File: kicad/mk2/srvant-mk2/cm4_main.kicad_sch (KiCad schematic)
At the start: 71 parts, among them J10 HDMI connector, J11 USB A, J6 Conn_02x05_Odd_Even, J8 Bus_M.2_Socket_M, J9 ARJM11, U13 74AHC1G04, U14 AP22653W6, U16 FSUSB42MUX, U17 PCF85063AT/AAZ, U18 74LVC1G07SE-7, U19 TPD4EUSB30, U20 TPD4EUSB30, U21 74LVC1G07SE-7, U23 SLB9670VQ20FW785XTMA1, U24 74AHC1G08, Y3 X32K768S301

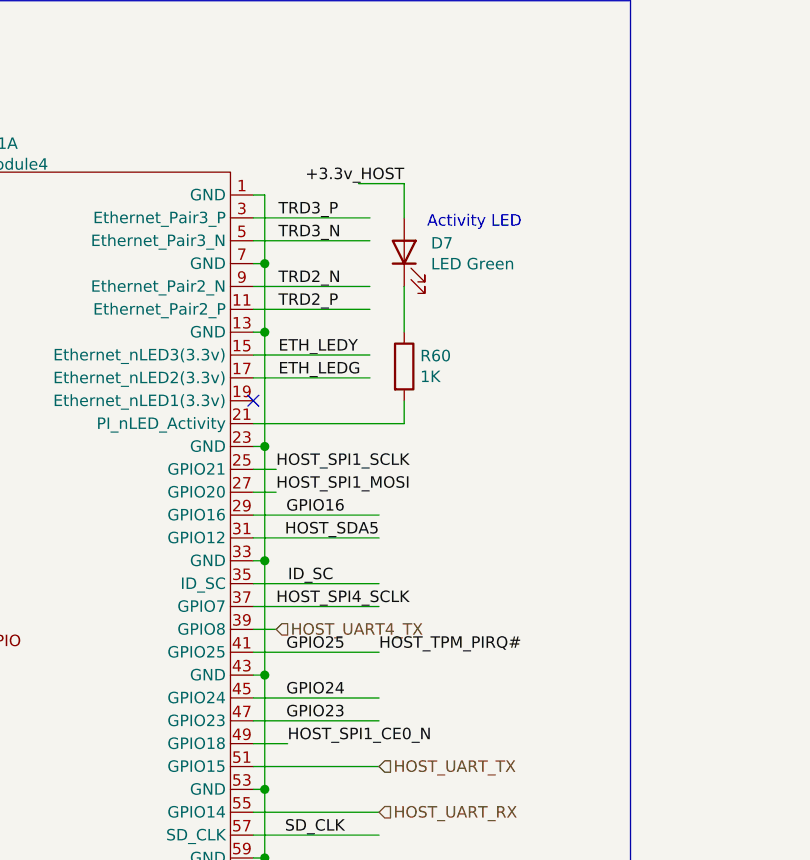
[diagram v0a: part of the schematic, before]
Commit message: reroute diff pairs
Reroute all diff pairs after another run with the jlcpcb calculator.
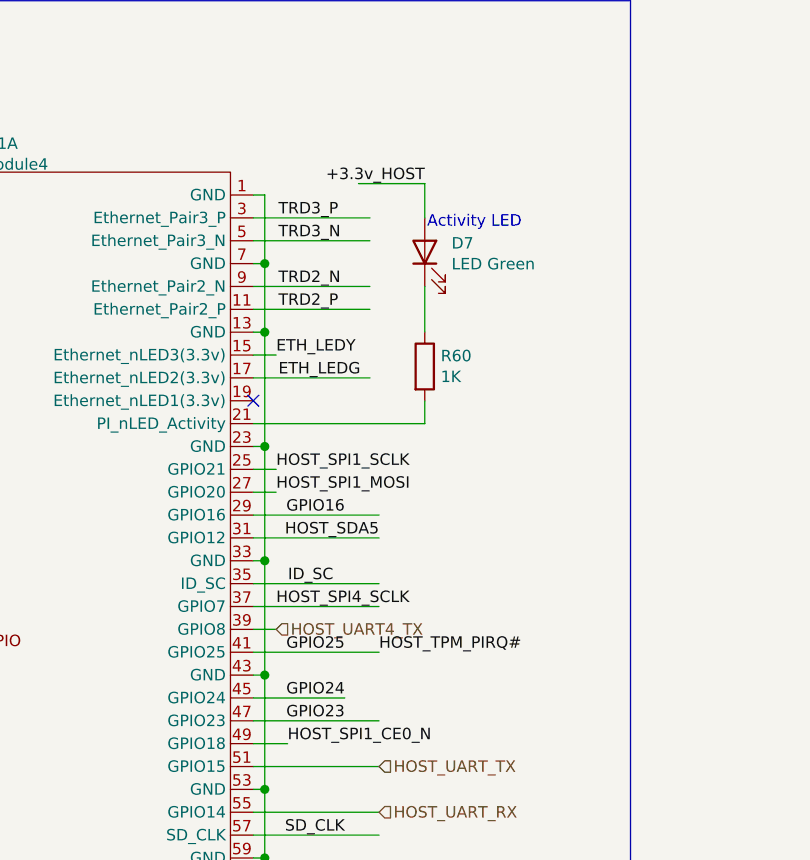
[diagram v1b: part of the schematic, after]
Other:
- moved on the sheet: D7, R60

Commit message: lot's of small updates
* fix the quartz footprint
* fix wrong inductor in pcie power unit
* fix lots of descriptions,uids
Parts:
- C102, C87, C98: Field4 Farnell -> (none); Field5 2611911 -> (none); Field6 RM EMK105 B7104KV-F -> (none); Field7 TAIYO YUDEN EUROPE GMBH -> (none); Field8 110091611 -> (none); farnell# (none) -> 3582682; manf# (none) -> GCM155R71C104KA55D; mouser# (none) -> 81-GCM155R71C104KA5D
- C42, C86, C93: farnell# (none) -> 3013481; manf# (none) -> CL21B105KAFNNNE
- C70, C75, C77, C79, C81, C83, C85, C92: Field5 490-14381-1-ND -> 490-10505-1-ND; Field6 GRM21BR71A106KA73L -> GRM21BC8YA106KE11L
- C74: Field4 Mouser -> (none); Field5 ECASD40J107M015K00 -> (none); mouser# (none) -> ECASD40J107M015K00
- C84, C91, C99: farnell# (none) -> 2812395; manf# (none) -> 885012207033
- C94: footprint Capacitor_SMD:C_0805_2012Metric -> Capacitor_SMD:C_0402_1005Metric; manf# (none) -> GRT155C81A105KE01D; mouser# (none) -> 81-GRT155C81A105KE1D
- FB8, FB9: farnell# (none) -> 4236024
- U13: farnell# (none) -> 1893806
- U14: farnell# (none) -> 3755402; manf# (none) -> AP22653W6-7
- U23: farnell# (none) -> 3404700
- U24: footprint Package_TO_SOT_SMD:SOT-23-5_HandSoldering -> Package_TO_SOT_SMD:SOT-23-5; farnell# (none) -> 3120306
- Y3: footprint Crystal:Crystal_SMD_3215-2Pin_3.2x1.5mm -> PCM_Crystal_AKL:Crystal_SMD_2012-2Pin_2.0x1.2mm; Field7 AEL -> (none); digikey# (none) -> 535-14101-2-ND; manf# (none) -> ABS06W-32.768KHZ-K-2-T

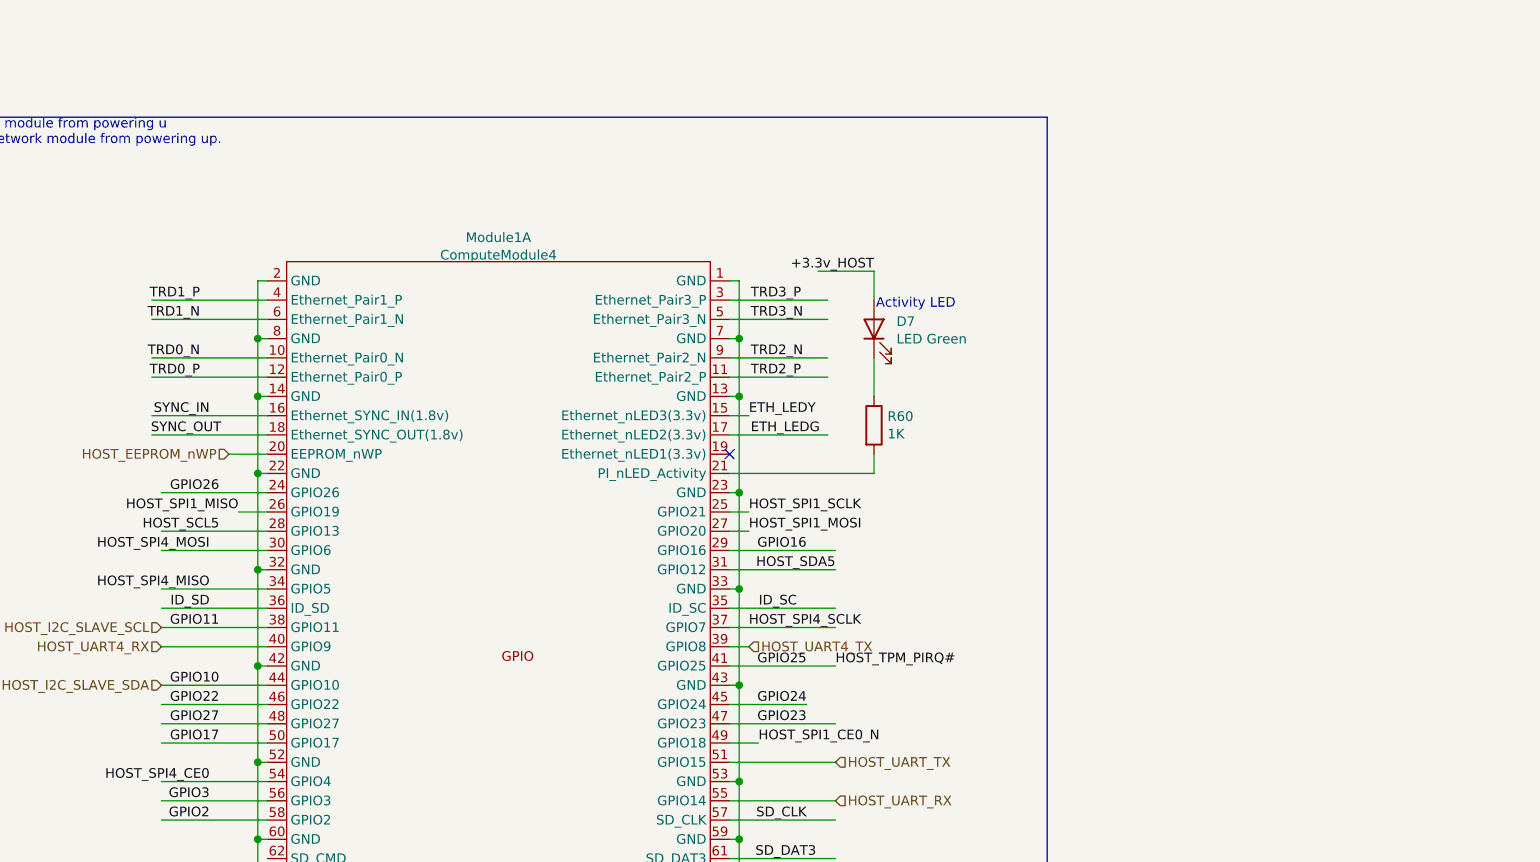
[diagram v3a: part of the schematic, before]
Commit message: add jtag pads, improve power lines
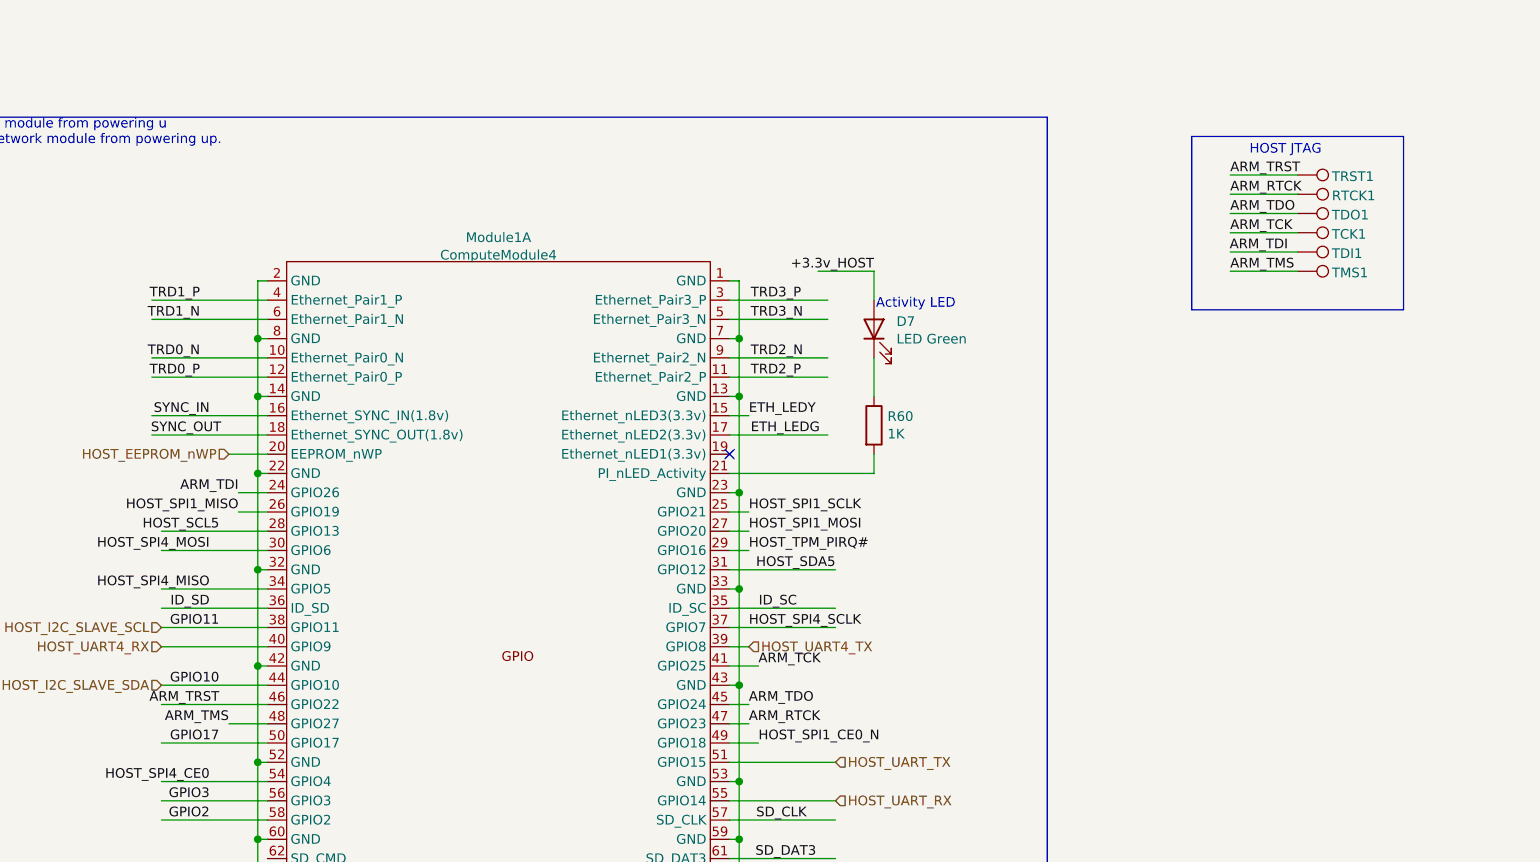
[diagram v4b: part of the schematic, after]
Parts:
- added RTCK1: RTCK, TestPoint:TestPoint_Pad_D1.0mm, symbol Connector:TestPoint
- added TCK1: TCK, TestPoint:TestPoint_Pad_D1.0mm, symbol Connector:TestPoint
- added TDI1: TDI, TestPoint:TestPoint_Pad_D1.0mm, symbol Connector:TestPoint
- added TDO1: TDO, TestPoint:TestPoint_Pad_D1.0mm, symbol Connector:TestPoint
- added TMS1: TMS, TestPoint:TestPoint_Pad_D1.0mm, symbol Connector:TestPoint
- added TRST1: TRST, TestPoint:TestPoint_Pad_D1.0mm, symbol Connector:TestPoint
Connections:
- net GPIO16 renamed HOST_TPM_PIRQ#
- net HOST_TPM_PIRQ#: now also U23.18 (PIRQ#)
- net GPIO22 renamed ARM_TRST
- net ARM_TRST: now also TRST1.1
- net GPIO23 renamed ARM_RTCK
- net ARM_RTCK: now also RTCK1.1
- net GPIO24 renamed ARM_TDO
- net ARM_TDO: now also TDO1.1
- net GPIO25 renamed ARM_TCK
- net ARM_TCK: now also TCK1.1; no longer U23.18 (PIRQ#)
- net GPIO26 renamed ARM_TDI
- net ARM_TDI: now also TDI1.1
- net GPIO27 renamed ARM_TMS
- net ARM_TMS: now also TMS1.1
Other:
- note added: "HOST JTAG"

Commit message: bmc usb id pin fix
ID pin is supposed to be unconnected on a peripheral device.
Connect usb_detect pin to VBUS using voltage divider (like in cm4 doc).
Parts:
- TP18: footprint TestPoint:TestPoint_Pad_1.0x1.0mm -> TestPoint:TestPoint_Pad_D1.0mm

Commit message: redesign for the next version
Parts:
- removed FB9: 220R, Resistor_SMD:R_0402_1005Metric, symbol Device:FerriteBead_Small
- removed R58: 2.2K, Resistor_SMD:R_0402_1005Metric, symbol Device:R
- removed TP12: 3v3_PCIe, TestPoint:TestPoint_Pad_D1.0mm, symbol Connector:TestPoint
- removed U16: FSUSB42MUX, footprints:FSUSB42UMX, symbol CM4IO:FSUSB42MX
- added C67, C68: 100n, Capacitor_SMD:C_0402_1005Metric, symbol Device:C
- added FB4: 220R, Resistor_SMD:R_0402_1005Metric, symbol Device:FerriteBead_Small
- added JP1, JP7: SolderJumper_2_Open, Jumper:SolderJumper-2_P1.3mm_Open_RoundedPad1.0x1.5mm, symbol Jumper:SolderJumper_2_Open
- added R54: 2.2K, Resistor_SMD:R_0402_1005Metric, symbol Device:R
- added R78: 10K, Resistor_SMD:R_0402_1005Metric, symbol Device:R
- added TP20, TP21, TP22: PCIe_nRST, TestPoint:TestPoint_Pad_D1.0mm, symbol Connector:TestPoint
- added U15: FSUSB42MUX, Package_SO:MSOP-10_3x3mm_P0.5mm, symbol Interface_USB:FSUSB42MUX
- C102, C42, C83, C84, C85, C86, C87, C91, C92, C93, C98, C99: footprint Capacitor_SMD:C_0805_2012Metric -> Capacitor_SMD:C_0402_1005Metric
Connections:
- net +3.3v_HOST: no longer C94.1, C95.2, C96.2, C97.2, D7.2 (A), D8.2 (A), J9.11 (LED2+), J9.13 (LED1+), R75.2, R76.1, U18.5 (VCC), U23.1 (NCI/VDD), U23.14 (NCI/VDD), U23.22 (VDD), U23.8 (VDD)
- net +5v_HOST: no longer C89.1, R57.2, R59.2, U13.5 (VCC), U21.5 (VCC), U24.5 (VCC)
- net GLOBAL_EN: now also JP1.1 (A), TP20.1; no longer Module1.99 (Global_EN)
- net GND: now also FB4.2, R54.2, U15.10 (~{OE}), U15.5 (GND)
- net HOST_GLOBAL_EN: now also U24.1, R78.1; no longer U24.2
- net HOST_RUN_PG: now also JP7.2 (B), TP21.1; no longer Module1.92 (RUN_PG)
- net HOST_USB_N: now also U15.8 (HSD2-)
- net HOST_USB_P: now also U15.9 (HSD2+)
- net PCIE_RX_N: now also C68.1; no longer J8.41 (PERn0/SATA-B+)
- net PCIE_RX_P: now also C67.1; no longer J8.43 (PERp0/SATA-B-)
- net PCIE_TX_N: now also J8.41 (PERn0/SATA-B+); no longer J8.47 (PETn0/SATA-A-)
- net PCIE_TX_P: now also J8.43 (PERp0/SATA-B-); no longer J8.49 (PETp0/SATA-A+)
- net USB2_N: now also U15.4 (D-)
- net USB2_P: now also U15.3 (D+)
- net USB_DEMUX_SELECT: now also R54.1, TP22.1, U15.2 (SEL)
- net USB_OUT_N: now also U15.6 (HSD1-)
- net USB_OUT_P: now also U15.7 (HSD1+)
- net nRTC_INT: now also U24.2; no longer U24.1
- net at J11.4 (GND), J11.5 (Shield): now also FB4.1
- net +3.3v_HOST_PCIe renamed +3v3_AUX
- net +3v3_AUX: now also C89.1, C94.1, C95.2, C96.2, C97.2, D7.2 (A), D8.2 (A), J9.11 (LED2+), J9.13 (LED1+), R57.2, R59.2, R75.2, R76.1, U13.5 (VCC), U18.5 (VCC), U21.5 (VCC), U23.1 (NCI/VDD), U23.14 (NCI/VDD), U23.22 (VDD), U23.8 (VDD), U24.5 (VCC), R78.2, U15.1 (VCC)
- new net: JP1.2 (B), Module1.99 (Global_EN)
- new net: JP7.1 (A), Module1.92 (RUN_PG)
- new net PET0_N: C68.2, J8.47 (PETn0/SATA-A-)
- new net PET0_P: C67.2, J8.49 (PETp0/SATA-A+)
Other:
- note added: "2.13. Global_EN Pulling this pin low puts the CM4 in the lowest possible power down state. After software shutdown Global_EN needs to be pulled low for > 1ms to restart the power system on the CM4. 2.14. RUN_PG This pin when high signals that the CM4 has started. Driving this pin low resets the module, this should be done with caution as if files on a filesystem are open they will not be closed 2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"
- note added: "510K was used for the 5v power, recalculate for 3.3v!"
- note added: "TODO: connect nEXTRST to BMC nEXTRST Output Driven low during reset Driven high (CM4_3.3V) once CM4 CPU has started to boot"
- note added: "TX and RX could have PN swaps to improve routing"
- note removed: "Should FSUSB42MUX be powered by the "external" +3.3v provided by BMC (always ON) ?"
- moved on the sheet: H1, H2, H3, TP14, TP15

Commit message: state
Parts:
- added J13, J14: Conn_01x03, Connector_PinHeader_2.54mm:PinHeader_1x03_P2.54mm_Vertical, symbol Connector_Generic:Conn_01x03
- added R80: 10K, Resistor_SMD:R_0402_1005Metric, symbol Device:R
- R54: value 2.2K -> 10K; Field4 Farnell -> (none); Field5 9239278 -> (none); Field6 RK73G1ETQTP2201D -> (none); Field7 KOA EUROPE GMBH -> (none); Field8 120889581 -> (none); Part Description Resistor 2.2K M1005 1% 63mW -> (none)
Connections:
- net +3v3_AUX: now also R54.2
- net GND: now also J13.1 (Pin_1), R80.1; no longer R54.2
- net HOST_UART_RX: now also J13.3 (Pin_3)
- net HOST_UART_TX: now also J13.2 (Pin_2)
- net USB_DEMUX_SELECT: now also J14.2 (Pin_2); no longer R54.1
- new net: J14.1 (Pin_1), R54.1
- new net: J14.3 (Pin_3), R80.2

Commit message: v1.5 draft
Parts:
- removed H1, H2, H3: MountingHole, MountingHole:MountingHole_2.5mm_Pad_TopOnly, symbol Mechanical:MountingHole
- added C58: 100n, Capacitor_SMD:C_0402_1005Metric, symbol Device:C
- added U8: ASEK-32.768KHZ-L-R-T, Crystal:Crystal_SMD_3225-4Pin_3.2x2.5mm, symbol CM5IO:ASEK-32.768KHZ-L-R-T
- J10, RTCK1, TCK1, TDI1, TDO1, TMS1, TRST1: now not fitted; now left out of the parts list
- J8: footprint footprints:1-2199230-5 -> footprints:M.2 M Key socket_rpi
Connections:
- net +3v3_AUX: now also C58.1, U8.1 (EN), U8.4 (VDD)
- net GND: now also C58.2, U8.2 (GND)
- net at J8.68 (SUSCLK): now also U8.3 (Out)
- no-connect marks 74 -> 73
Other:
- note added: "NOTE: SUSCLK should be connected to 32khz clock. nRST might have to be connected to GND through R CLKREQ/WAKE do I need to pull up? https://forums.raspberrypi.com/viewtopic.php?t=361437#p2168693 RPI CM5 schematic does not have any of the pullup/pulldown resistors https://forums.raspberrypi.com/viewtopic.php?t=361437#p2168693"
- moved on the sheet: C102, C42, C67, C68, C83, C84, C85, C86, C87, C91, C92, C93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
